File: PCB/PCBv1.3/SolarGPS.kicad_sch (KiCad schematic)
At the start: 58 parts, among them J1 Conn_01x10_Female, J2 Solar1+, J3 GND, J4 Conn_02x03_Odd_Even, J5 Solar2+, J6 GND, J7 Screw_Terminal_01x01, J8 Conn_01x04_Male, U1 STM32L011G3Ux, U2 MAX-M10Q, U5 BQ25505, U6 LIS3DH, U7 TPS63802, Y1 32.768

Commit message: Move symbols to lib
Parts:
- C14: footprint Veridian-Library-KiCad:SCCT20E106SRB -> Heliograph:SCCT20E106SRB
- J1: footprint Margo_Lib:LS013B7DH03 -> Heliograph:LS013B7DH03
- L3: footprint Margo_Lib:744031220 -> Heliograph:744031220
- U5: footprint Package_DFN_QFN:QFN-20-1EP_3.5x3.5mm_P0.5mm_EP2x2mm -> Package_DFN_QFN:Texas_VQFN-RGR-20; symbol MargoGeneral:BQ25505 -> Heliograph:BQ25505
- U7: footprint Margo_Lib:VREG_TPS63802DLAR -> Heliograph:VREG_TPS63802DLAR; symbol SolarGPS-rescue:TPS63802-VeridianDesigns -> Heliograph:TPS63802-VeridianDesigns
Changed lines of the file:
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@@
       (effects (font (size 1.27 1.27)) (justify left))
     )
-    (property "Footprint" "Margo_Lib:LS013B7DH03" (id 2) (at 194.056 143.002 0)
+    (property "Footprint" "Heliograph:LS013B7DH03" (id 2) (at 194.056 143.002 0)
       (effects (font (size 1.27 1.27)) hide)
     )
@@
     (pin "1")
   )
-  (symbol (lib_id "SolarGPS-rescue:TPS63802-VeridianDesigns") (at 115.57 184.15 0) (unit 1)
+  (symbol (lib_id "Heliograph:TPS63802-VeridianDesigns") (at 115.57 184.15 0) (unit 1)
     (in_bom yes) (on_board yes)
     (property "Reference" "U7" (id 0) (at 123.19 186.0042 0))
     (property "Value" "TPS63802" (id 1) (at 123.19 188.3156 0))
-    (property "Footprint" "Margo_Lib:VREG_TPS63802DLAR" (id 2) (at 115.57 184.15 0)
+    (property "Footprint" "Heliograph:VREG_TPS63802DLAR" (id 2) (at 115.57 184.15 0)
       (effects (font (size 1.27 1.27)) hide)
     )
@@
     (property "Reference" "L3" (id 0) (at 36.83 153.67 90))
     (property "Value" "22uH" (id 1) (at 36.83 155.575 90))
-    (property "Footprint" "Margo_Lib:744031220" (id 2) (at 36.83 157.48 0)
+    (property "Footprint" "Heliograph:744031220" (id 2) (at 36.83 157.48 0)
       (effects (font (size 1.27 1.27)) hide)
     )
@@
     (pin "2")
   )
-  (symbol (lib_id "MargoGeneral:BQ25505") (at 47.625 184.15 0) (unit 1)
+  (symbol (lib_id "Heliograph:BQ25505") (at 47.625 184.15 0) (unit 1)
     (in_bom yes) (on_board yes)
     (property "Reference" "U5" (id 0) (at 59.055 151.765 0))
     (property "Value" "BQ25505" (id 1) (at 59.055 154.0764 0))
-    (property "Footprint" "Package_DFN_QFN:QFN-20-1EP_3.5x3.5mm_P0.5mm_EP2x2mm" (id 2) (at 47.625 184.15 0)
+    (property "Footprint" "Package_DFN_QFN:Texas_VQFN-RGR-20" (id 2) (at 47.625 184.15 0)
       (effects (font (size 1.27 1.27)) hide)
     )
@@
       (effects (font (size 1.27 1.27)) (justify left))
     )
-    (property "Footprint" "Veridian-Library-KiCad:SCCT20E106SRB" (id 2) (at 93.0402 173.355 0)
+    (property "Footprint" "Heliograph:SCCT20E106SRB" (id 2) (at 93.0402 173.355 0)
       (effects (font (size 1.27 1.27)) hide)
     )
@@
     )
     (path "/00000000-0000-0000-0000-000061be4ac8"
-      (reference "C14") (unit 1) (value "10F") (footprint "Veridian-Library-KiCad:SCCT20E106SRB")
+      (reference "C14") (unit 1) (value "10F") (footprint "Heliograph:SCCT20E106SRB")
     )
     (path "/00000000-0000-0000-0000-000061b114b5"
@@
     )
     (path "/00000000-0000-0000-0000-000061a063d0"
-      (reference "J1") (unit 1) (value "Conn_01x10_Female") (footprint "Margo_Lib:LS013B7DH03")
+      (reference "J1") (unit 1) (value "Conn_01x10_Female") (footprint "Heliograph:LS013B7DH03")
     )
     (path "/00000000-0000-0000-0000-000061c94a66"
@@
     )
     (path "/00000000-0000-0000-0000-000061adda7b"
-      (reference "L3") (unit 1) (value "22uH") (footprint "Margo_Lib:744031220")
+      (reference "L3") (unit 1) (value "22uH") (footprint "Heliograph:744031220")
     )
     (path "/e2846743-92e2-465a-8c71-d71294501e9b"
@@
     )
     (path "/00000000-0000-0000-0000-000061addaa4"
-      (reference "U5") (unit 1) (value "BQ25505") (footprint "Package_DFN_QFN:QFN-20-1EP_3.5x3.5mm_P0.5mm_EP2x2mm")
+      (reference "U5") (unit 1) (value "BQ25505") (footprint "Package_DFN_QFN:Texas_VQFN-RGR-20")
     )
     (path "/00000000-0000-0000-0000-000061a5a316"
@@
     )
     (path "/00000000-0000-0000-0000-000061a98429"
-      (reference "U7") (unit 1) (value "TPS63802") (footprint "Margo_Lib:VREG_TPS63802DLAR")
+      (reference "U7") (unit 1) (value "TPS63802") (footprint "Heliograph:VREG_TPS63802DLAR")
     )
     (path "/36e706fb-88f0-49d7-89e1-dda073c7a7ac"

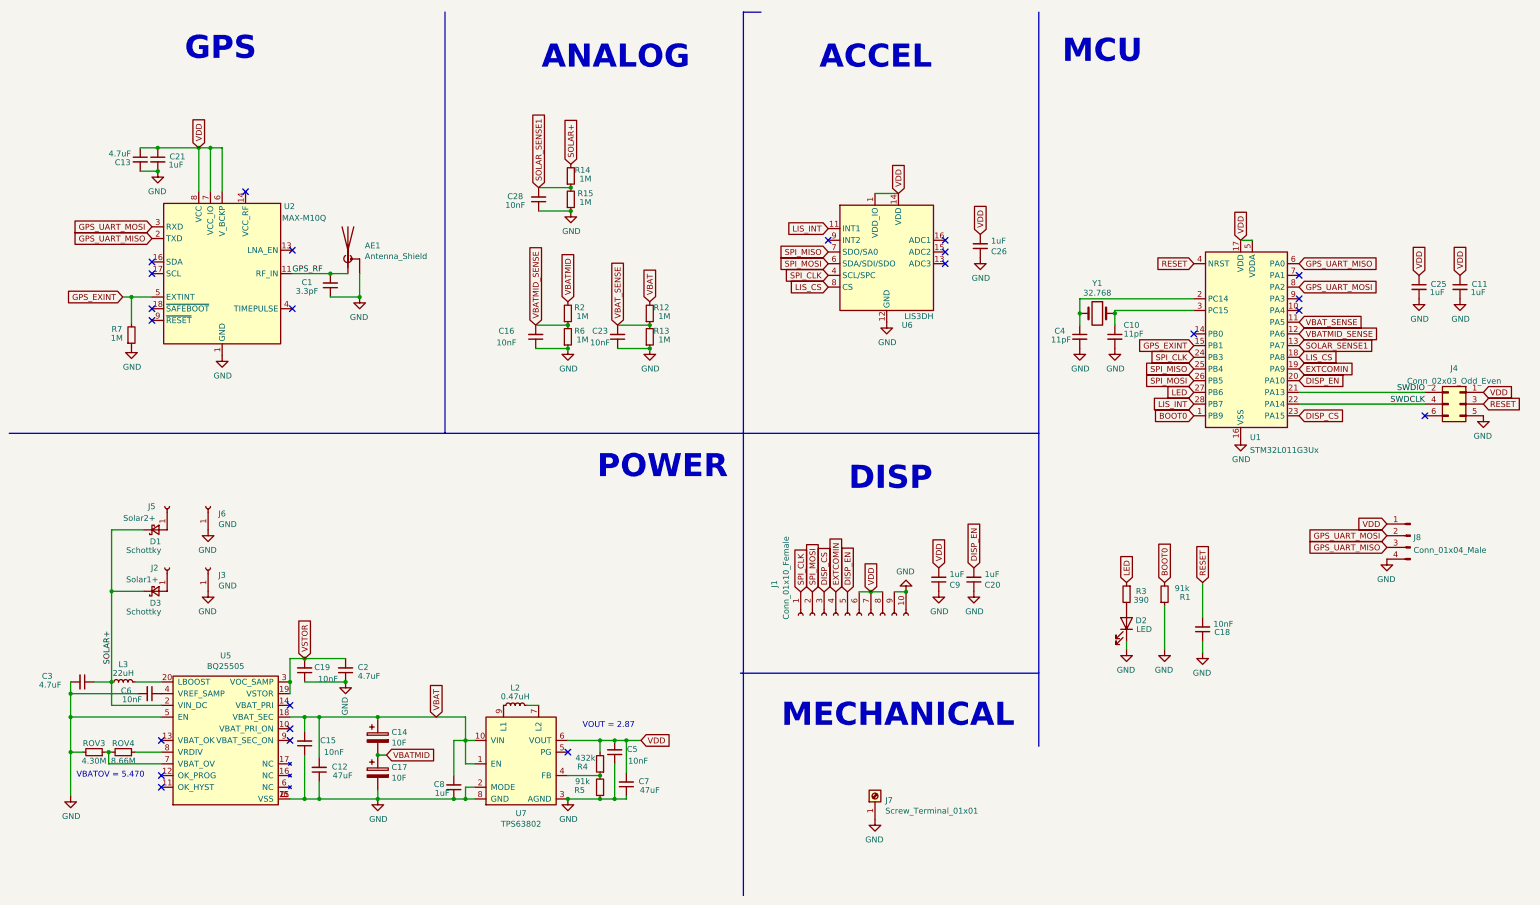
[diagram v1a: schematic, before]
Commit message: Drop MPPT buck for diode cost
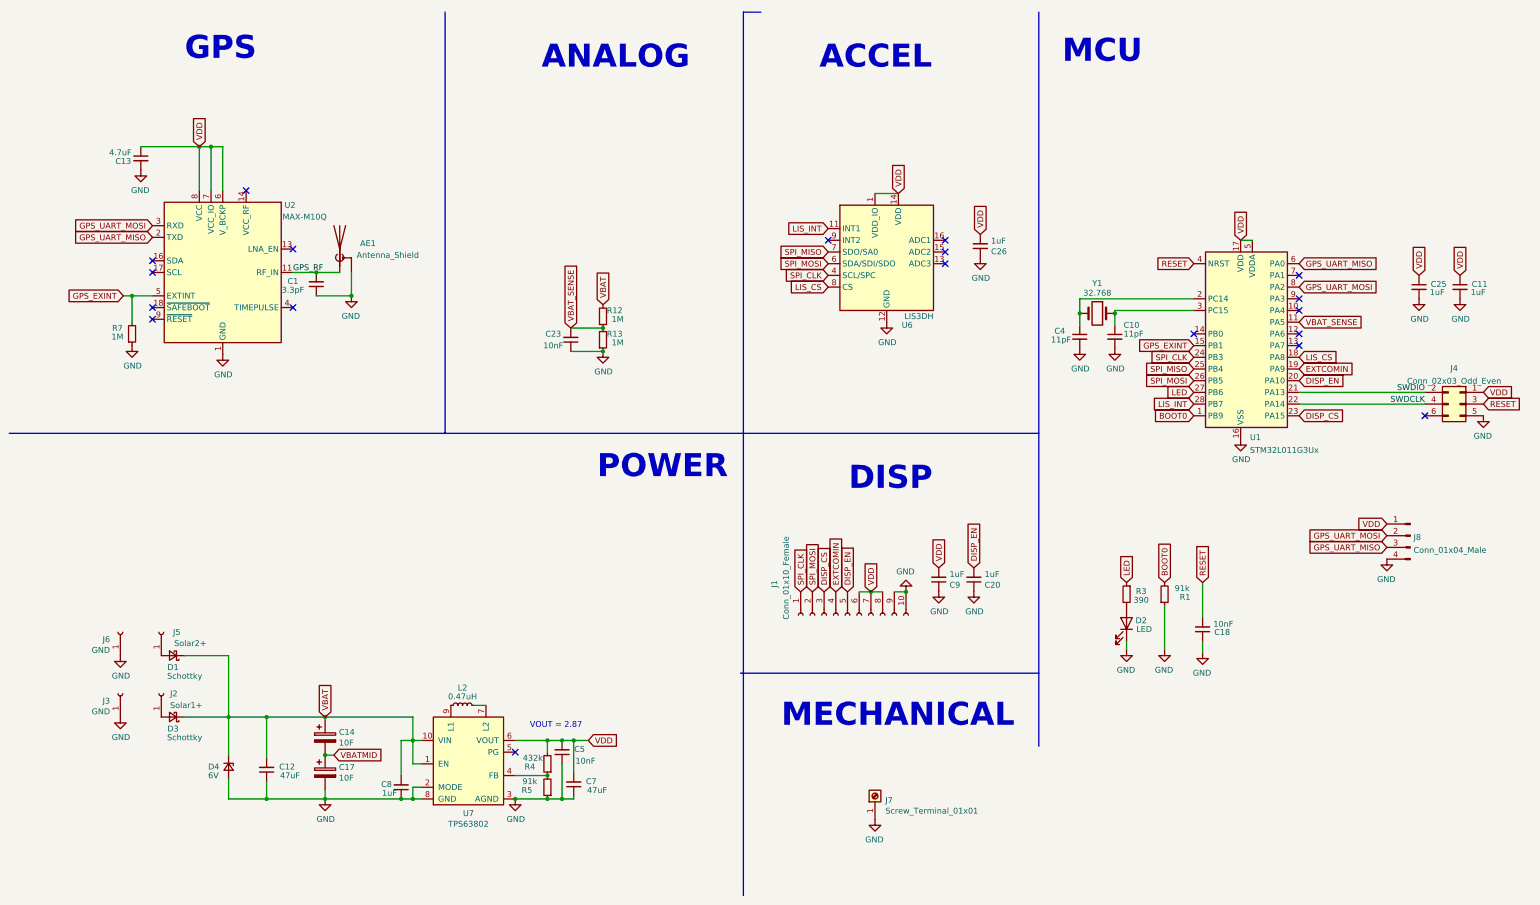
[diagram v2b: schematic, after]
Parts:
- removed C15, C16, C19, C28, C6: 10nF, Capacitor_SMD:C_0603_1608Metric, symbol Device:C_Small
- removed C2, C3: 4.7uF, Capacitor_SMD:C_0805_2012Metric, symbol Device:C_Small
- removed C21: 1uF, Capacitor_SMD:C_0603_1608Metric, symbol Device:C_Small
- removed L3: 22uH, Heliograph:744031220, symbol Device:L_Small
- removed R14, R15, R2, R6: 1M, Resistor_SMD:R_0603_1608Metric, symbol Device:R_Small
- removed ROV3: 4.30M, Resistor_SMD:R_0603_1608Metric, symbol Device:R_Small
- removed ROV4: 8.66M, Resistor_SMD:R_0603_1608Metric, symbol Device:R_Small
- removed U5: BQ25505, Package_DFN_QFN:Texas_VQFN-RGR-20, symbol Heliograph:BQ25505
- added D4: 6V, Diode_SMD:D_SOD-123, symbol Device:D_Zener_Small
- J4: footprint Connector:Tag-Connect_TC2030-IDC-NL_2x03_P1.27mm_Vertical -> Connector:Tag-Connect_TC2030-IDC-FP_2x03_P1.27mm_Vertical
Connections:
- net SOLAR+ is gone; now on net VBAT: D1.1 (K), D3.1 (K)
- net GND: now also D4.2 (A)
- net VBAT: now also D4.1 (K)
- net SOLAR_SENSE1: no longer names the net of U1.13 (PA7)
- net VBATMID_SENSE: no longer names the net of U1.12 (PA6)
- no-connect marks 23 -> 19
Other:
- note removed: "VBATOV = 5.470"
- moved on the sheet: AE1, C1, C12, C14, C17, C23, C5, C7, C8, D1, D3, J2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

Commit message: Change LCD
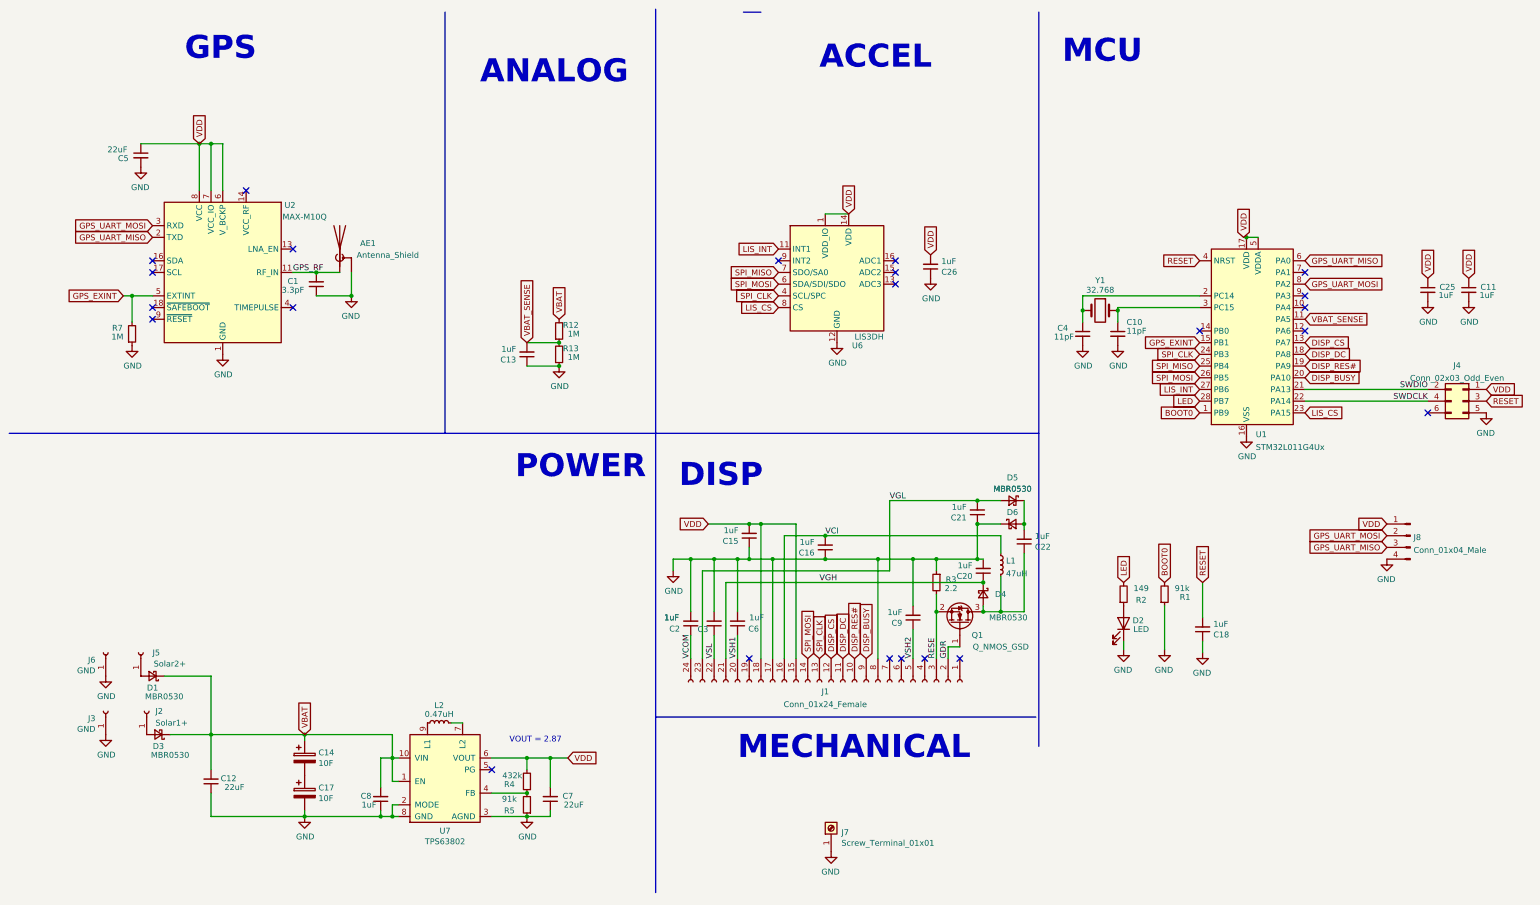
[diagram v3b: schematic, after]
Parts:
- removed C23: 10nF, Capacitor_SMD:C_0603_1608Metric, symbol Device:C_Small
- removed D4: 6V, Diode_SMD:D_SOD-123, symbol Device:D_Zener_Small
- removed J1: Conn_01x10_Female, Heliograph:LS013B7DH03, symbol Connector:Conn_01x10_Female
- removed U1: STM32L011G3Ux, Package_DFN_QFN:QFN-28_4x4mm_P0.5mm, symbol MCU_ST_STM32L0:STM32L011G3Ux
- added C15, C16, C2, C21, C22, C3, C6: 1uF, Capacitor_SMD:C_0603_1608Metric, symbol Device:C_Small
- added D4, D5, D6: MBR0530, Diode_SMD:D_SOD-123, symbol Device:D_Schottky_Small
- added J1: Conn_01x24_Female, Connector_FFC-FPC:Hirose_FH12-24S-0.5SH_1x24-1MP_P0.50mm_Horizontal, symbol Connector:Conn_01x24_Female
- added L1: 47uH, Inductor_SMD:L_Taiyo-Yuden_NR-40xx, symbol Device:L_Small
- added Q1: Q_NMOS_GSD, Package_TO_SOT_SMD:SOT-23, symbol Device:Q_NMOS_GSD
- added R2: 149, Resistor_SMD:R_0603_1608Metric, symbol Device:R_Small
- added U1: STM32L011G4Ux, Package_DFN_QFN:QFN-28_4x4mm_P0.5mm, symbol MCU_ST_STM32L0:STM32L011G4Ux
- C12, C7: value 47uF -> 22uF; footprint Capacitor_SMD:C_1206_3216Metric -> Capacitor_SMD:C_0603_1608Metric; Part (none) -> GRM187R61A226ME15
- C13: value 4.7uF -> 1uF; footprint Capacitor_SMD:C_0805_2012Metric -> Capacitor_SMD:C_0603_1608Metric
- C14: footprint Heliograph:SCCT20E106SRB -> Heliograph:SCCT20E106SRB_SMD
- C17: footprint Veridian-Library-KiCad:SCCT20E106SRB -> Heliograph:SCCT20E106SRB_SMD
- C18: value 10nF -> 1uF
- C5: value 10nF -> 22uF; Part (none) -> GRM187R61A226ME15
- D1, D3: value Schottky -> MBR0530; footprint Diode_SMD:D_SOD-323_HandSoldering -> Diode_SMD:D_SOD-123
- J4: footprint Connector:Tag-Connect_TC2030-IDC-FP_2x03_P1.27mm_Vertical -> Connector:Tag-Connect_TC2030-IDC-NL_2x03_P1.27mm_Vertical
- R3: value 390 -> 2.2
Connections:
- net DISP_EN is gone; now on net GND: C20.2
- net BOOT0: now also U1.1 (PB9)
- net DISP_CS: now also J1.12 (Pin_12), U1.13 (PA7)
- net GND: now also C13.1, C5.2, C9.2, R3.1, C15.1, C16.1, C2.2, C21.1, C3.2, C6.2, D6.1 (K), J1.17 (Pin_17), J1.8 (Pin_8), U1.16 (VSS); no longer C13.2, C20.1, C5.1, C9.1
- net GPS_EXINT: now also U1.15 (PB1)
- net GPS_UART_MISO: now also U1.6 (PA0)
- net GPS_UART_MOSI: now also U1.8 (PA2)
- net LED: now also R2.2, U1.28 (PB7); no longer R3.1
- net LIS_CS: now also U1.23 (PA15)
- net LIS_INT: now also U1.27 (PB6)
- net RESET: now also U1.4 (NRST)
- net SPI_CLK: now also J1.13 (Pin_13), U1.24 (PB3)
- net SPI_MISO: now also U1.25 (PB4)
- net SPI_MOSI: now also J1.14 (Pin_14), U1.26 (PB5)
- net SWDCLK: now also U1.22 (PA14)
- net SWDIO: now also U1.21 (PA13)
- net VBAT_SENSE: now also C13.2, U1.11 (PA5)
- net VDD: now also C5.1, C15.2, J1.15 (Pin_15), J1.18 (Pin_18), U1.17 (VDD), U1.5 (VDDA); no longer C13.1, C5.2, C9.2
- net at D2.2 (A): now also R2.1; no longer R3.2
- net at C4.1, Y1.2: now also U1.2 (PC14)
- net at C10.1, Y1.1: now also U1.3 (PC15)
- net VBATMID: no longer names the net of C14.2, C17.1
- new net: C22.1, D4.2 (A), L1.2, Q1.3 (D)
- new net: C22.2, D5.1 (K), D6.2 (A)
- new net DISP_BUSY: J1.9 (Pin_9), U1.20 (PA10)
- new net DISP_DC: J1.11 (Pin_11), U1.18 (PA8)
- new net DISP_RES#: J1.10 (Pin_10), U1.19 (PA9)
- new net GDR: J1.2 (Pin_2), Q1.1 (G)
- new net RESE: J1.3 (Pin_3), Q1.2 (S), R3.2
- new net VCI: C16.2, J1.16 (Pin_16), L1.1
- new net VCOM: C2.1, J1.24 (Pin_24)
- new net VGH: C20.1, D4.1 (K), J1.21 (Pin_21)
- new net VGL: C21.2, D5.2 (A), J1.23 (Pin_23)
- new net VSH1: C6.1, J1.20 (Pin_20)
- new net VSH2: C9.1, J1.5 (Pin_5)
- new net VSL: C3.1, J1.22 (Pin_22)
- no-connect marks 19 -> 23
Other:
- moved on the sheet: C10, C11, C14, C17, C25, C26, C4, C7, C8, C9, D1, D2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
